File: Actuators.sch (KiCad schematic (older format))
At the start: 7 parts, among them M1 Motor_DC, M2 Motor_DC, U4 DRV8847_TSSOP

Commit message: Correct schematics after review
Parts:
- removed D3: PUMP_LED, LED_SMD:LED_0603_1608Metric, symbol Device:LED
- removed R6: 510, Resistor_SMD:R_0402_1005Metric, symbol Device:R
- added C18: 0.1 uF, symbol Device:C_Small
- added D3, D4, D5, D6: 1N4007, Diode_THT:D_DO-41_SOD81_P10.16mm_Horizontal, symbol Diode:1N4007
- added M2: Output Connector PUMP2, symbol Motor:Motor_DC
- added M4: Output Connector Solenoid 2, symbol Motor:Motor_DC
- CONN5, CONN6: value SERVO -> SERVO, Molex Picoblade 3 pin
- M1: value Motor_DC -> Output Connector PUMP1
- M3: renamed from M2; value Motor_DC -> Output Connector Solenoid 1
- U4: value DRV8847_TSSOP -> DRV8847PWR, Digikey part 296-53425-1-ND
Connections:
- net labels added: PUMP_SOLENOID_ENABLE, SERVO_POWER, SOLENOID_IN1, SOLENOID_IN2
- net labels removed: PUMP_ENABLE, PUMP_LED
- wire segments 15 -> 50
- no-connect marks 5 -> 1
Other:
- moved on the sheet: M1, M3

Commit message: Cleanup labels, motor placement, power labels
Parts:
- removed CONN5, CONN6: SERVO, Molex Picoblade 3 pin, symbol _connectors:SERVO
- added C15: CP, symbol Device:CP
- added J1: SERVO PWR, symbol Connector_Generic:Conn_01x02
- added M5, M6: Motor_Servo, symbol Motor:Motor_Servo
- M1: value Output Connector PUMP1 -> PUMP1
- M2: value Output Connector PUMP2 -> PUMP2
- M3: value Output Connector Solenoid 1 -> Solenoid 1
- M4: value Output Connector Solenoid 2 -> Solenoid 2
- U4: value DRV8847PWR, Digikey part 296-53425-1-ND -> DRV8847PWR; Digikey (none) -> 296-53425-1-ND
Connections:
- net labels added: +BATT
- net labels removed: ACTUATOR_GND, ACTUATOR_POWER, SERVO_POWER
- wire segments 50 -> 44
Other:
- moved on the sheet: D3, D4, D5, D6, M1, M2, M3, M4

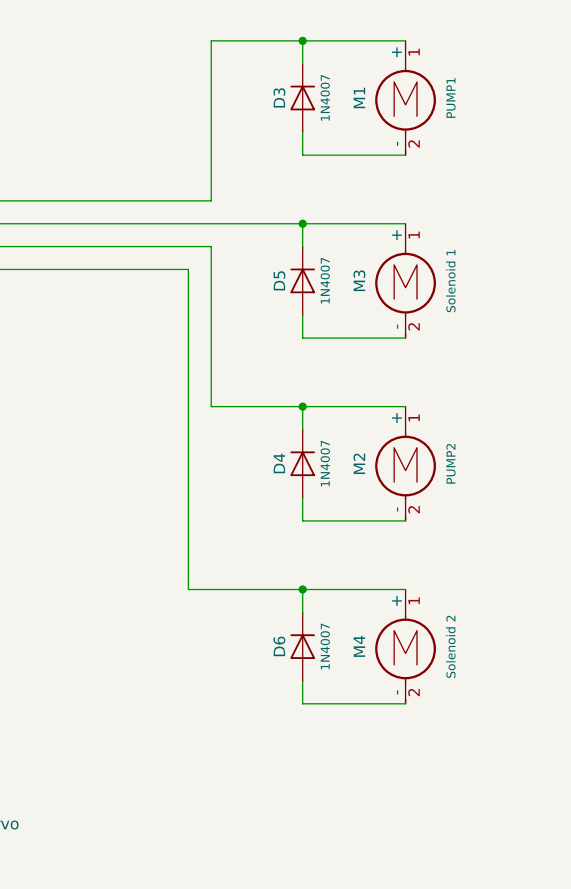
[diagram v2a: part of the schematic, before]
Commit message: Change to Schottky flyback diode, update valve symbol
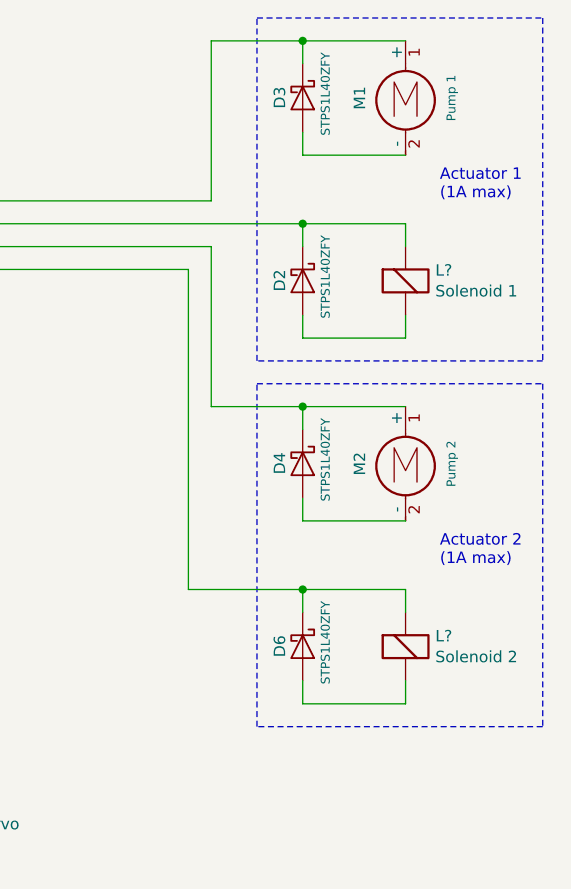
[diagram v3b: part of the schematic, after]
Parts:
- removed D3, D4, D5, D6: 1N4007, Diode_THT:D_DO-41_SOD81_P10.16mm_Horizontal, symbol Diode:1N4007
- removed M3: Solenoid 1, symbol Motor:Motor_DC
- removed M4: Solenoid 2, symbol Motor:Motor_DC
- added D2, D3, D4, D6: STPS1L40ZFY, Diode_SMD:D_SOD-123F, symbol Device:D_Schottky
- added L?: Solenoid 1, symbol Device:Electromagnetic_Actor
- added L?: Solenoid 2, symbol Device:Electromagnetic_Actor
- M1: value PUMP1 -> Pump 1
- M2: value PUMP2 -> Pump 2
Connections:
- wire segments 44 -> 48
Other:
- note added: "Actuator 1\n(1A max)"
- note added: "Actuator 2\n(1A max)"
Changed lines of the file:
@@
 P 7450 2150
 F 0 "M1" V 7250 2100 50  0000 C CNN
-F 1 "PUMP1" V 7650 2100 39  0000 C CNN
+F 1 "Pump 1" V 7650 2100 39  0000 C CNN
 F 2 "" H 7450 2060 50  0001 C CNN
 F 3 "~" H 7450 2060 50  0001 C CNN
 	1    7450 2150
-	1    0    0    -1
-$EndComp
-$Comp
-L Diode:1N4007 D5
-U 1 1 5E2D59F1
-P 7000 3000
-F 0 "D5" H 7000 2900 50  0000 C CNN
-F 1 "1N4007" H 7000 3100 39  0000 C CNN
-F 2 "Diode_THT:D_DO-41_SOD81_P10.16mm_Horizontal" H 7000 2825 50  0001 C CNN
-F 3 "http://www.vishay.com/docs/88503/1n4001.pdf" H 7000 3000 50  0001 C CNN
-	1    7000 3000
-	0    1    1    0
-$EndComp
-$Comp
-L Motor:Motor_DC M4
-U 1 1 5E2BC831
-P 7450 4550
-F 0 "M4" V 7250 4500 50  0000 C CNN
-F 1 "Solenoid 2" V 7650 4500 39  0000 C CNN
-F 2 "" H 7450 4460 50  0001 C CNN
-F 3 "~" H 7450 4460 50  0001 C CNN
-	1    7450 4550
 	1    0    0    -1
 $EndComp
@@
 P 7450 3750
 F 0 "M2" V 7250 3700 50  0000 C CNN
-F 1 "PUMP2" V 7650 3700 39  0000 C CNN
+F 1 "Pump 2" V 7650 3700 39  0000 C CNN
 F 2 "" H 7450 3660 50  0001 C CNN
 F 3 "~" H 7450 3660 50  0001 C CNN
@@
 	1    0    0    -1
 $EndComp
-$Comp
-L Diode:1N4007 D6
-U 1 1 5E2D9DB9
-P 7000 4600
-F 0 "D6" H 7000 4500 50  0000 C CNN
-F 1 "1N4007" H 7000 4700 39  0000 C CNN
-F 2 "Diode_THT:D_DO-41_SOD81_P10.16mm_Horizontal" H 7000 4425 50  0001 C CNN
-F 3 "http://www.vishay.com/docs/88503/1n4001.pdf" H 7000 4600 50  0001 C CNN
-	1    7000 4600
-	0    1    1    0
-$EndComp
-$Comp
-L Diode:1N4007 D4
-U 1 1 5E2D5A4A
-P 7000 3800
-F 0 "D4" H 7000 3700 50  0000 C CNN
-F 1 "1N4007" H 7000 3900 39  0000 C CNN
-F 2 "Diode_THT:D_DO-41_SOD81_P10.16mm_Horizontal" H 7000 3625 50  0001 C CNN
-F 3 "http://www.vishay.com/docs/88503/1n4001.pdf" H 7000 3800 50  0001 C CNN
-	1    7000 3800
-	0    1    1    0
-$EndComp
-$Comp
-L Motor:Motor_DC M3
-U 1 1 5E24A20B
-P 7450 2950
-F 0 "M3" V 7250 2900 50  0000 C CNN
-F 1 "Solenoid 1" V 7650 2900 39  0000 C CNN
-F 2 "" H 7450 2860 50  0001 C CNN
-F 3 "~" H 7450 2860 50  0001 C CNN
-	1    7450 2950
-	1    0    0    -1
-$EndComp
-Wire Wire Line
-	5250 2750 7000 2750
 Wire Wire Line
 	5250 2650 6600 2650
@@
 Wire Wire Line
 	6500 4350 7000 4350
-$Comp
-L Diode:1N4007 D3
-U 1 1 5E2CA0FB
-P 7000 2200
-F 0 "D3" H 7000 2100 50  0000 C CNN
-F 1 "1N4007" H 7000 2300 39  0000 C CNN
-F 2 "Diode_THT:D_DO-41_SOD81_P10.16mm_Horizontal" H 7000 2025 50  0001 C CNN
-F 3 "http://www.vishay.com/docs/88503/1n4001.pdf" H 7000 2200 50  0001 C CNN
-	1    7000 2200
-	0    1    1    0
-$EndComp
 Wire Wire Line
 	7000 2050 7000 1950
@@
 Wire Wire Line
 	7000 2450 7450 2450
-Wire Wire Line
-	7000 3150 7000 3250
-Wire Wire Line
-	7000 3250 7450 3250
-Wire Wire Line
-	7000 2850 7000 2750
-Connection ~ 7000 2750
-Wire Wire Line
-	7000 2750 7450 2750
 Wire Wire Line
 	7000 3650 7000 3550
@@
 Wire Wire Line
 	7000 4850 7450 4850
+$Comp
+L Device:D_Schottky D3
+U 1 1 5E5D4248
+P 7000 2200
+F 0 "D3" H 6950 2100 50  0000 L CNN
+F 1 "STPS1L40ZFY" H 6800 2300 39  0000 L CNN
+F 2 "Diode_SMD:D_SOD-123F" H 7000 2200 50  0001 C CNN
+F 3 "https://www.st.com/resource/en/datasheet/stps1l40-y.pdf" H 7000 2200 50  0001 C CNN
+F 4 "497-17153-1-ND" V 7000 2200 50  0001 C CNN "Digikey"
+	1    7000 2200
+	0    1    1    0
+$EndComp
+$Comp
+L Device:D_Schottky D4
+U 1 1 5E5D7906
+P 7000 3800
+F 0 "D4" H 6950 3700 50  0000 L CNN
+F 1 "STPS1L40ZFY" H 6800 3900 39  0000 L CNN
+F 2 "Diode_SMD:D_SOD-123F" H 7000 3800 50  0001 C CNN
+F 3 "https://www.st.com/resource/en/datasheet/stps1l40-y.pdf" H 7000 3800 50  0001 C CNN
+F 4 "497-17153-1-ND" V 7000 3800 50  0001 C CNN "Digikey"
+	1    7000 3800
+	0    1    1    0
+$EndComp
+$Comp
+L Device:D_Schottky D6
+U 1 1 5E5D9416
+P 7000 4600
+F 0 "D6" H 6950 4500 50  0000 L CNN
+F 1 "STPS1L40ZFY" H 6800 4700 39  0000 L CNN
+F 2 "Diode_SMD:D_SOD-123F" H 7000 4600 50  0001 C CNN
+F 3 "https://www.st.com/resource/en/datasheet/stps1l40-y.pdf" H 7000 4600 50  0001 C CNN
+F 4 "497-17153-1-ND" V 7000 4600 50  0001 C CNN "Digikey"
+	1    7000 4600
+	0    1    1    0
+$EndComp
+$Comp
+L Device:D_Schottky D2
+U 1 1 5E5D5F10
+P 7000 3000
+F 0 "D2" H 6950 2900 50  0000 L CNN
+F 1 "STPS1L40ZFY" H 6800 3100 39  0000 L CNN
+F 2 "Diode_SMD:D_SOD-123F" H 7000 3000 50  0001 C CNN
+F 3 "https://www.st.com/resource/en/datasheet/stps1l40-y.pdf" H 7000 3000 50  0001 C CNN
+F 4 "497-17153-1-ND" V 7000 3000 50  0001 C CNN "Digikey"
+	1    7000 3000
+	0    1    1    0
+$EndComp
+Wire Wire Line
+	7000 3150 7000 3250
+Wire Wire Line
+	7000 3250 7450 3250
+Wire Wire Line
+	7000 2750 7450 2750
+Wire Wire Line
+	5250 2750 7000 2750
+Connection ~ 7000 2750
+Wire Wire Line
+	7000 2850 7000 2750
+$Comp
+L Device:Electromagnetic_Actor L?
+U 1 1 5E5DF558
+P 7450 3050
+F 0 "L?" H 7580 3146 50  0000 L CNN
+F 1 "Solenoid 1" H 7580 3055 50  0000 L CNN
+F 2 "" V 7425 3150 50  0001 C CNN
+F 3 "~" V 7425 3150 50  0001 C CNN
+	1    7450 3050
+	1    0    0    -1
+$EndComp
+Wire Wire Line
+	7450 2750 7450 2850
+Wire Wire Line
+	7450 3150 7450 3250
+$Comp
+L Device:Electromagnetic_Actor L?
+U 1 1 5E5E309E
+P 7450 4650
+F 0 "L?" H 7580 4746 50  0000 L CNN
+F 1 "Solenoid 2" H 7580 4655 50  0000 L CNN
+F 2 "" V 7425 4750 50  0001 C CNN
+F 3 "~" V 7425 4750 50  0001 C CNN
+	1    7450 4650
+	1    0    0    -1
+$EndComp
+Wire Wire Line
+	7450 4350 7450 4450
+Wire Wire Line
+	7450 4750 7450 4850
+Text Notes 7600 2650 0    50   ~ 0
+Actuator 1\n(1A max)
+Wire Notes Line
+	8050 1850 8050 3350
+Wire Notes Line
+	8050 3350 6800 3350
+Wire Notes Line
+	6800 3350 6800 1850
+Wire Notes Line
+	6800 1850 8050 1850
+Wire Notes Line
+	8050 3450 8050 4950
+Wire Notes Line
+	8050 4950 6800 4950
+Wire Notes Line
+	6800 4950 6800 3450
+Wire Notes Line
+	6800 3450 8050 3450
+Text Notes 7600 4250 0    50   ~ 0
+Actuator 2\n(1A max)
 $EndSCHEMATC

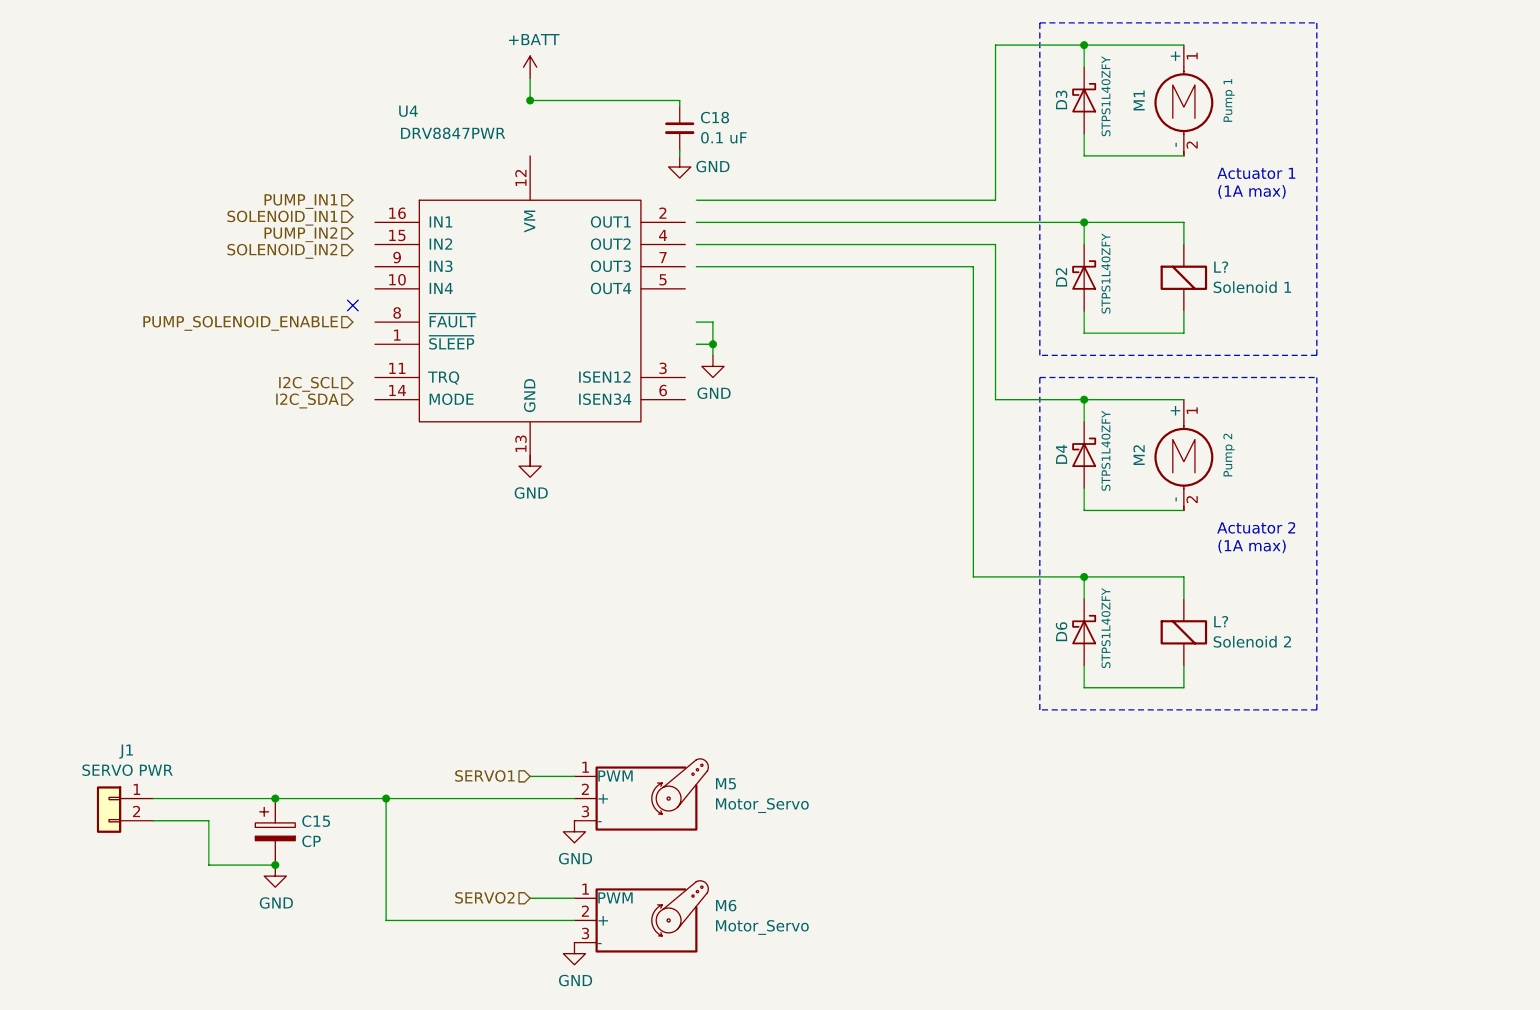
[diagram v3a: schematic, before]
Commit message: Clear component annotation
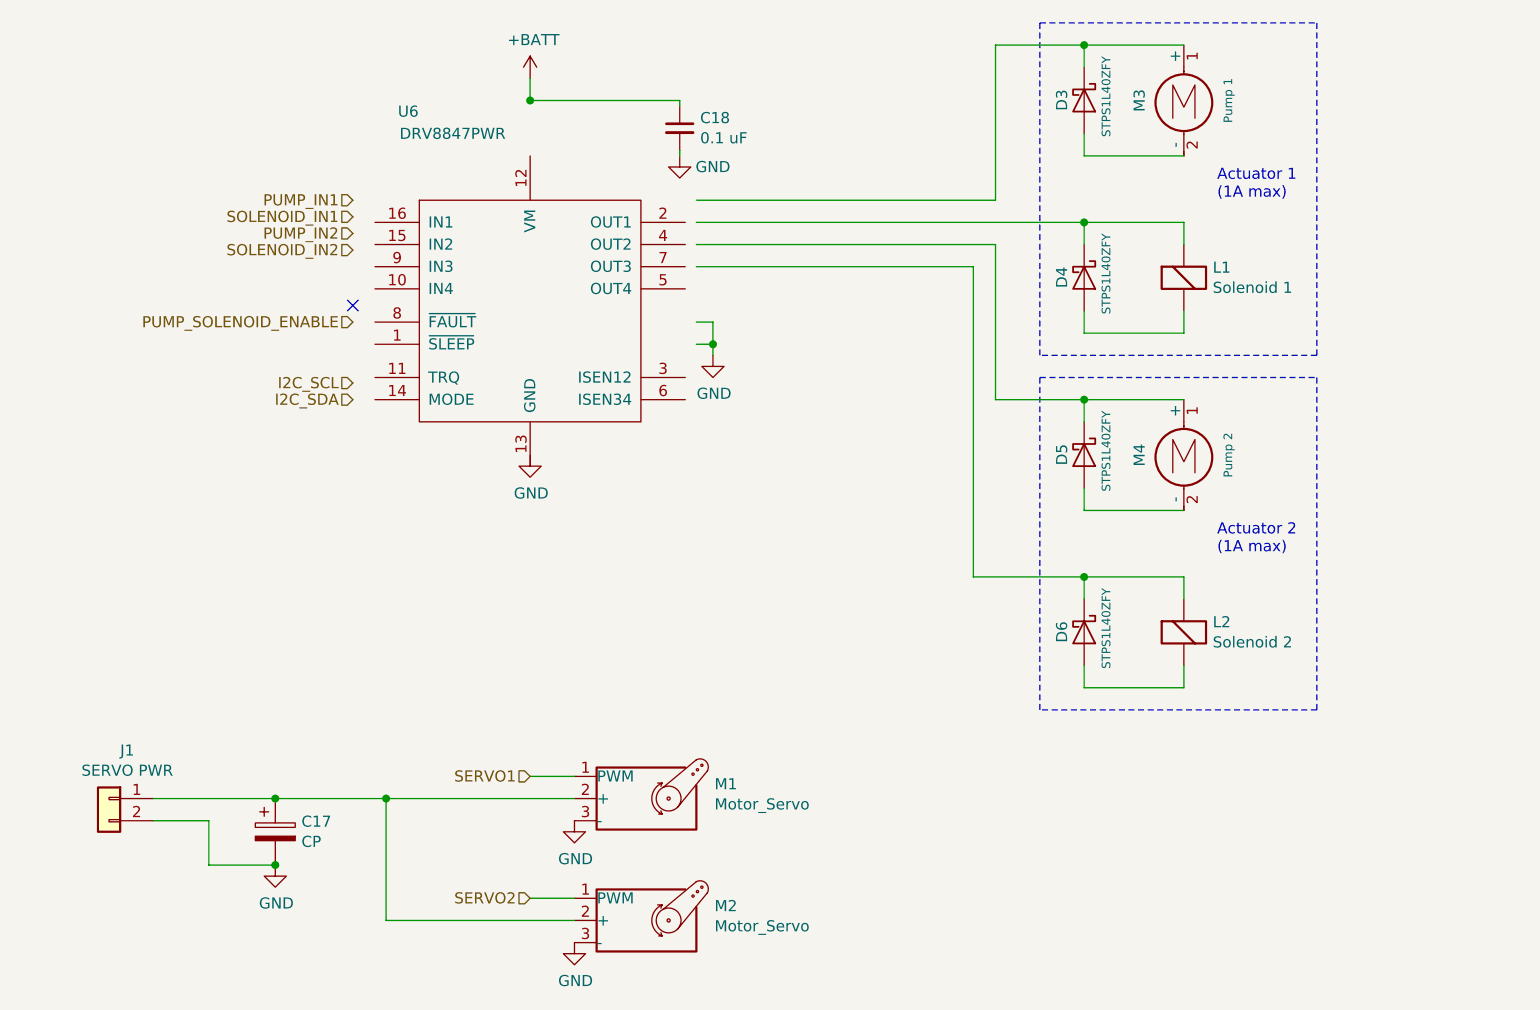
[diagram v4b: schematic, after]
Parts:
- gave numbers to parts that had none: 2
- renumbered C15 to C17, D2 to D4, D4 to D5, M5 to M1, M6 to M2, M1 to M3, M2 to M4, U4 to U6
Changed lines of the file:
@@
 NoConn ~ 3700 3125
 $Comp
-L power:GND #PWR026
+L power:GND #PWR035
 U 1 1 5E239CA6
 P 4500 3800
-F 0 "#PWR026" H 4500 3550 50  0001 C CNN
+F 0 "#PWR035" H 4500 3550 50  0001 C CNN
 F 1 "GND" H 4505 3627 50  0000 C CNN
 F 2 "" H 4500 3800 50  0001 C CNN
@@
 $EndComp
 $Comp
-L power:GND #PWR0107
+L power:GND #PWR039
 U 1 1 5E260916
 P 5325 3350
-F 0 "#PWR0107" H 5325 3100 50  0001 C CNN
+F 0 "#PWR039" H 5325 3100 50  0001 C CNN
 F 1 "GND" H 5330 3177 50  0000 C CNN
 F 2 "" H 5325 3350 50  0001 C CNN
@@
 $EndComp
 $Comp
-L power:GND #PWR021
+L power:GND #PWR038
 U 1 1 5E2FC82D
 P 5175 2450
-F 0 "#PWR021" H 5175 2200 50  0001 C CNN
+F 0 "#PWR038" H 5175 2200 50  0001 C CNN
 F 1 "GND" H 5325 2400 50  0000 C CNN
 F 2 "" H 5175 2450 50  0001 C CNN
@@
 	5175 2425 5175 2450
 $Comp
-L Motor:Motor_Servo M5
+L Motor:Motor_Servo M1
 U 1 1 5E37BD0B
 P 5000 5350
-F 0 "M5" H 5332 5415 50  0000 L CNN
+F 0 "M1" H 5332 5415 50  0000 L CNN
 F 1 "Motor_Servo" H 5332 5324 50  0000 L CNN
 F 2 "" H 5000 5160 50  0001 C CNN
@@
 $EndComp
 $Comp
-L Motor:Motor_Servo M6
+L Motor:Motor_Servo M2
 U 1 1 5E38464C
 P 5000 5900
-F 0 "M6" H 5332 5965 50  0000 L CNN
+F 0 "M2" H 5332 5965 50  0000 L CNN
 F 1 "Motor_Servo" H 5332 5874 50  0000 L CNN
 F 2 "" H 5000 5710 50  0001 C CNN
@@
 $EndComp
 $Comp
-L _power:DRV8847_TSSOP U4
+L _power:DRV8847_TSSOP U6
 U 1 1 5E23D2B5
 P 4500 3150
-F 0 "U4" H 3950 4050 50  0000 C CNN
+F 0 "U6" H 3950 4050 50  0000 C CNN
 F 1 "DRV8847PWR" H 4150 3950 50  0000 C CNN
 F 2 "" H 4500 3150 50  0001 C CNN
@@
 P 3350 5500
 AR Path="/5E3A79F5" Ref="C?"  Part="1"
-AR Path="/5E1FB153/5E3A79F5" Ref="C15"  Part="1"
-F 0 "C15" H 3468 5546 50  0000 L CNN
+AR Path="/5E1FB153/5E3A79F5" Ref="C17"  Part="1"
+F 0 "C17" H 3468 5546 50  0000 L CNN
 F 1 "CP" H 3468 5455 50  0000 L CNN
 F 2 "" H 3388 5350 50  0001 C CNN
@@
 P 3350 5650
 AR Path="/5E3A79FB" Ref="#PWR?"  Part="1"
-AR Path="/5E1FB153/5E3A79FB" Ref="#PWR0115"  Part="1"
-F 0 "#PWR0115" H 3350 5400 50  0001 C CNN
+AR Path="/5E1FB153/5E3A79FB" Ref="#PWR033"  Part="1"
+F 0 "#PWR033" H 3350 5400 50  0001 C CNN
 F 1 "GND" H 3355 5477 50  0000 C CNN
 F 2 "" H 3350 5650 50  0001 C CNN
@@
 P 4700 5450
 AR Path="/5E3D17A5" Ref="#PWR?"  Part="1"
-AR Path="/5E1FB153/5E3D17A5" Ref="#PWR0116"  Part="1"
-F 0 "#PWR0116" H 4700 5200 50  0001 C CNN
+AR Path="/5E1FB153/5E3D17A5" Ref="#PWR036"  Part="1"
+F 0 "#PWR036" H 4700 5200 50  0001 C CNN
 F 1 "GND" H 4705 5277 50  0000 C CNN
 F 2 "" H 4700 5450 50  0001 C CNN
@@
 P 4700 6000
 AR Path="/5E3D4696" Ref="#PWR?"  Part="1"
-AR Path="/5E1FB153/5E3D4696" Ref="#PWR0117"  Part="1"
-F 0 "#PWR0117" H 4700 5750 50  0001 C CNN
+AR Path="/5E1FB153/5E3D4696" Ref="#PWR037"  Part="1"
+F 0 "#PWR037" H 4700 5750 50  0001 C CNN
 F 1 "GND" H 4705 5827 50  0000 C CNN
 F 2 "" H 4700 6000 50  0001 C CNN
@@
 	4700 5250 4500 5250
 $Comp
-L power:+BATT #PWR0118
+L power:+BATT #PWR034
 U 1 1 5E3DDDE9
 P 4500 2100
-F 0 "#PWR0118" H 4500 1950 50  0001 C CNN
+F 0 "#PWR034" H 4500 1950 50  0001 C CNN
 F 1 "+BATT" H 4515 2273 50  0000 C CNN
 F 2 "" H 4500 2100 50  0001 C CNN
@@
 Connection ~ 4500 2200
 $Comp
-L Motor:Motor_DC M1
+L Motor:Motor_DC M3
 U 1 1 5E248EAA
 P 7450 2150
-F 0 "M1" V 7250 2100 50  0000 C CNN
+F 0 "M3" V 7250 2100 50  0000 C CNN
 F 1 "Pump 1" V 7650 2100 39  0000 C CNN
 F 2 "" H 7450 2060 50  0001 C CNN
@@
 $EndComp
 $Comp
-L Motor:Motor_DC M2
+L Motor:Motor_DC M4
 U 1 1 5E2BC872
 P 7450 3750
-F 0 "M2" V 7250 3700 50  0000 C CNN
+F 0 "M4" V 7250 3700 50  0000 C CNN
 F 1 "Pump 2" V 7650 3700 39  0000 C CNN
 F 2 "" H 7450 3660 50  0001 C CNN
@@
 $EndComp
 $Comp
-L Device:D_Schottky D4
+L Device:D_Schottky D5
 U 1 1 5E5D7906
 P 7000 3800
-F 0 "D4" H 6950 3700 50  0000 L CNN
+F 0 "D5" H 6950 3700 50  0000 L CNN
 F 1 "STPS1L40ZFY" H 6800 3900 39  0000 L CNN
 F 2 "Diode_SMD:D_SOD-123F" H 7000 3800 50  0001 C CNN
@@
 $EndComp
 $Comp
-L Device:D_Schottky D2
+L Device:D_Schottky D4
 U 1 1 5E5D5F10
 P 7000 3000
-F 0 "D2" H 6950 2900 50  0000 L CNN
+F 0 "D4" H 6950 2900 50  0000 L CNN
 F 1 "STPS1L40ZFY" H 6800 3100 39  0000 L CNN
 F 2 "Diode_SMD:D_SOD-123F" H 7000 3000 50  0001 C CNN
@@
 	7000 2850 7000 2750
 $Comp
-L Device:Electromagnetic_Actor L?
+L Device:Electromagnetic_Actor L1
 U 1 1 5E5DF558
 P 7450 3050
-F 0 "L?" H 7580 3146 50  0000 L CNN
+F 0 "L1" H 7580 3146 50  0000 L CNN
 F 1 "Solenoid 1" H 7580 3055 50  0000 L CNN
 F 2 "" V 7425 3150 50  0001 C CNN
@@
 	7450 3150 7450 3250
 $Comp
-L Device:Electromagnetic_Actor L?
+L Device:Electromagnetic_Actor L2
 U 1 1 5E5E309E
 P 7450 4650
-F 0 "L?" H 7580 4746 50  0000 L CNN
+F 0 "L2" H 7580 4746 50  0000 L CNN
 F 1 "Solenoid 2" H 7580 4655 50  0000 L CNN
 F 2 "" V 7425 4750 50  0001 C CNN
